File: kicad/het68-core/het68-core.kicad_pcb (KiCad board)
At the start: 6 copper layers, 160 x 100 mm, 134 parts, among them J1 MIC1, J11 PZ1, J12 PZ2, J13 PZ3, J14 PZ4, J2 MIC2, J3 MIC3, J4 MIC4, J5 MIC5, J6 MIC6, U1 RP2350B, U10 SN65LVDS047, U11 SN65LVDS047, U12 SN65LVDS047, U13 SN65LVDS32, U14 SN65LVDS32, U2 W25Q128JVSIQ, U3 APS6404L, U4 AP2112K-3.3, U5 AP2112K-1.8, U6 DRV8837C, U7 DPS310, U8 SHT40, U9 ADXL355, Y1 12MHz

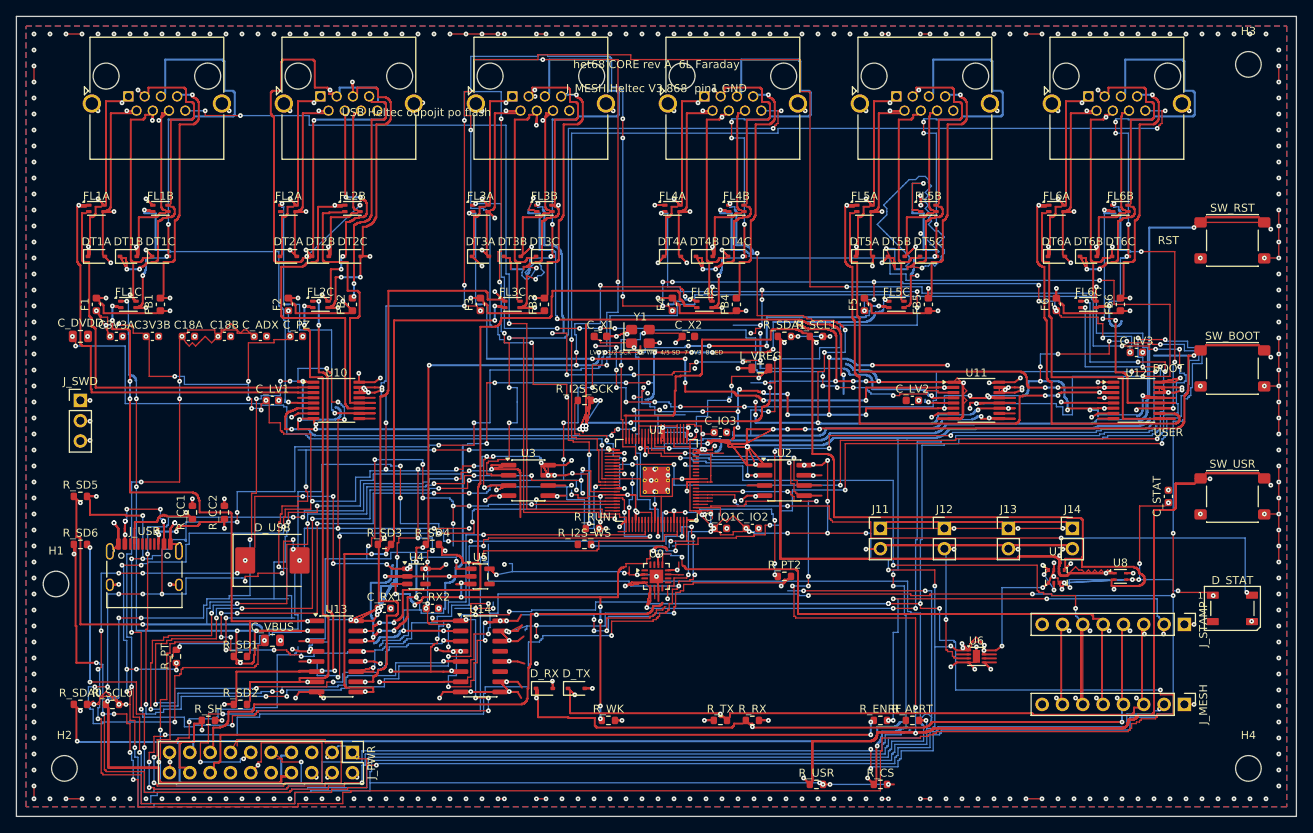
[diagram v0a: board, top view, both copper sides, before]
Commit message: Route the core with 0.15 mm vias and one 3.3 V plane.
JLCPCB drills 0.15 mm on 6 layers. A 0.30 mm via fits the 0.40 mm QFN pitch, and L4 under the RP2350 is now a single +3V3_DIG pour so those vias meet the plane. DRC reports no shorts and no clearance errors. Seventeen pairs stay open where the via ring leaves no 0.15 mm exit.

Co-authored-by: fedurca <fedurca@users.noreply.github.com>
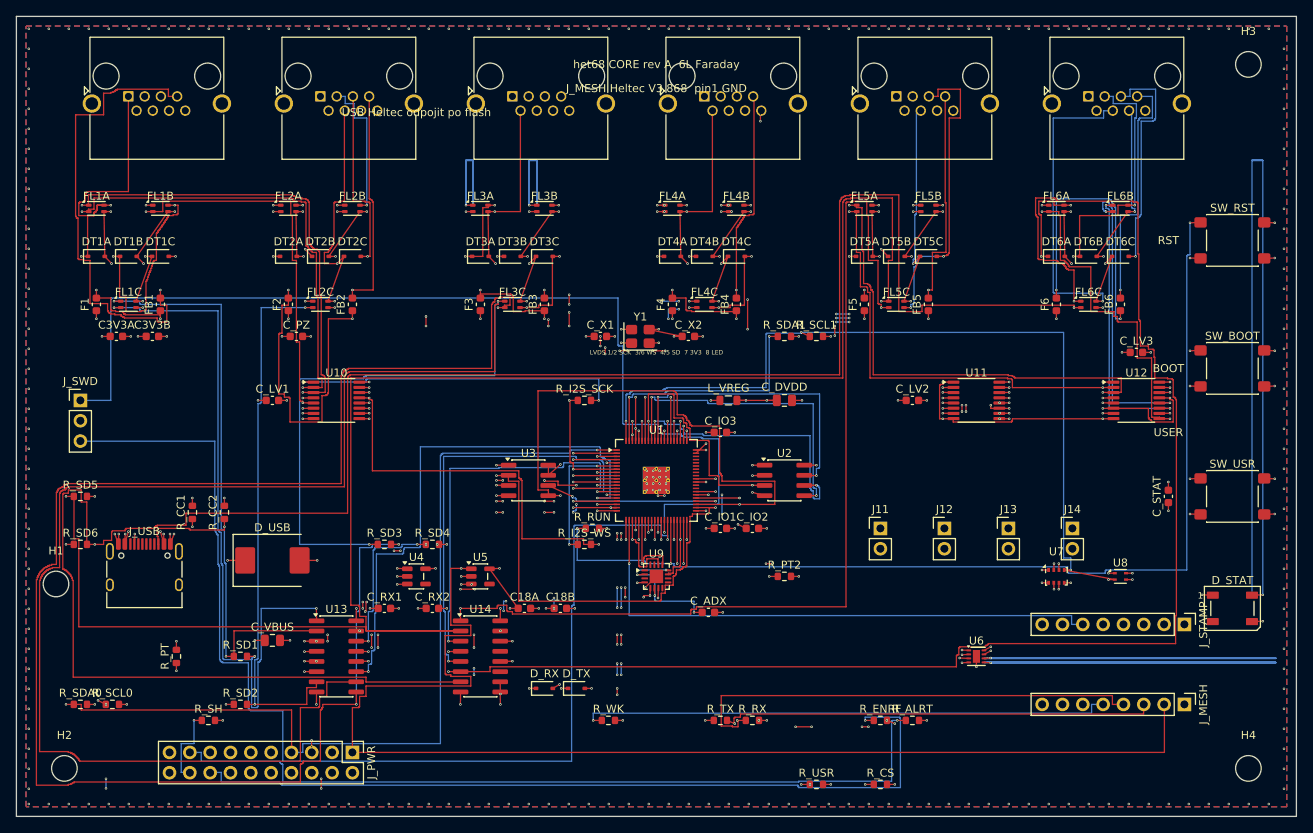
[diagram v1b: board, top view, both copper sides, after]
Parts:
- moved C_DVDD 88.4 mm to (96.0, 48.0)
- moved C_ADX 65.8 mm to (86.5, 74.5)
- moved C18A 54.0 mm to (63.5, 74.0)
- moved C18B 54.0 mm to (68.0, 74.0)
- moved L_VREG 5.66 mm to (89.0, 48.0)
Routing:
- net +3V3_DIG: track 1831.7 -> 74.2 mm, vias 164 -> 63
- net GND: track 663.1 -> 119.5 mm, vias 361 -> 290
- net PIEZO_IN1: track 2.95 -> 438.0 mm, vias 0 -> 2
- net PIEZO_IN2: track 11.4 -> 441.0 mm, vias 1 -> 2
- net SD2_P: track 80.1 -> 387.6 mm, vias 5 -> 3
- net I2S_SD5: track 351.5 -> 57.3 mm, vias 23 -> 2
- net +1V8_AUDIO: track 325.7 -> 44.0 mm, vias 13 -> 10
- net PSRAM_SO: track 280.0 -> 59.7 mm, vias 20 -> 2
- net RUN: track 344.2 -> 148.2 mm, vias 10 -> 4
- net +5V_ALWAYS: track 434.1 -> 244.5 mm, vias 20 -> 3
- net BURDEN_EN: track 186.0 -> 7.85 mm, vias 9 -> 1
- net SD6_P: track 557.1 -> 391.7 mm, vias 22 -> 3
- net I2C0_SCL: track 208.8 -> 52.8 mm, vias 14 -> 7
- net SWDIO: track 4.04 -> 149.5 mm
- net SD3_P: track 93.9 -> 230.1 mm, vias 3 -> 2
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- removed copper zone on In3.Cu, net +1V8_AUDIO
- removed copper zone on In3.Cu, net +5V_ALWAYS
